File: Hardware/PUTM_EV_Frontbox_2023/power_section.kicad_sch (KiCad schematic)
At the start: 40 parts, among them U19 TLV743P, U4 TLV743P, U5 TLV743P, U7 LM62440-Q1

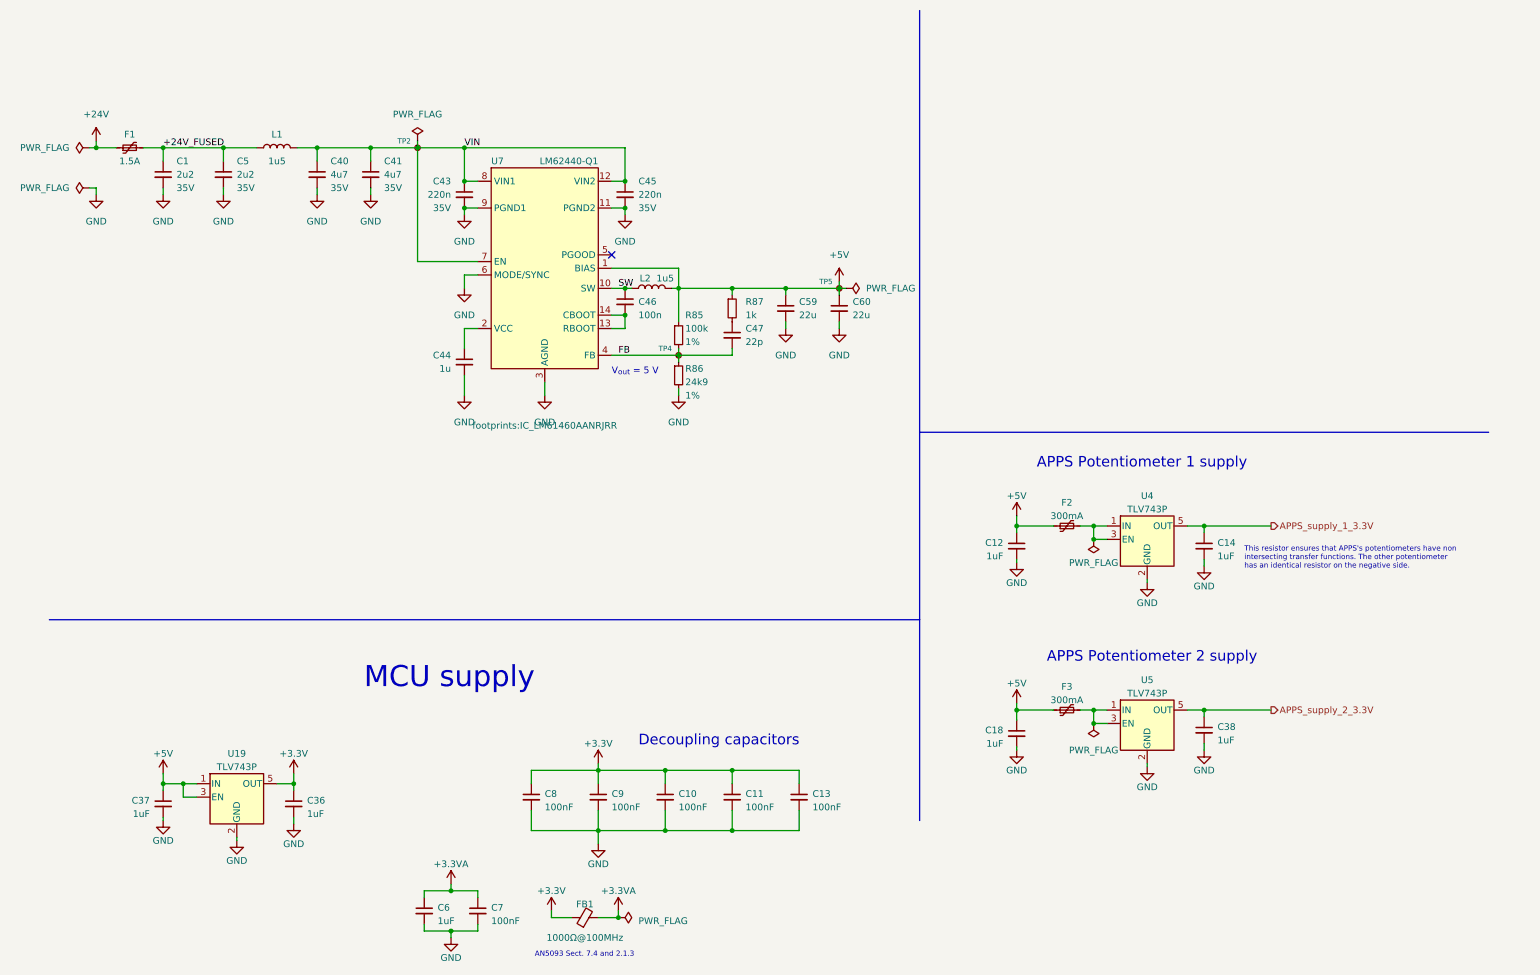
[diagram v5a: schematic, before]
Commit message: Added gearbox temperature sensors on schematic
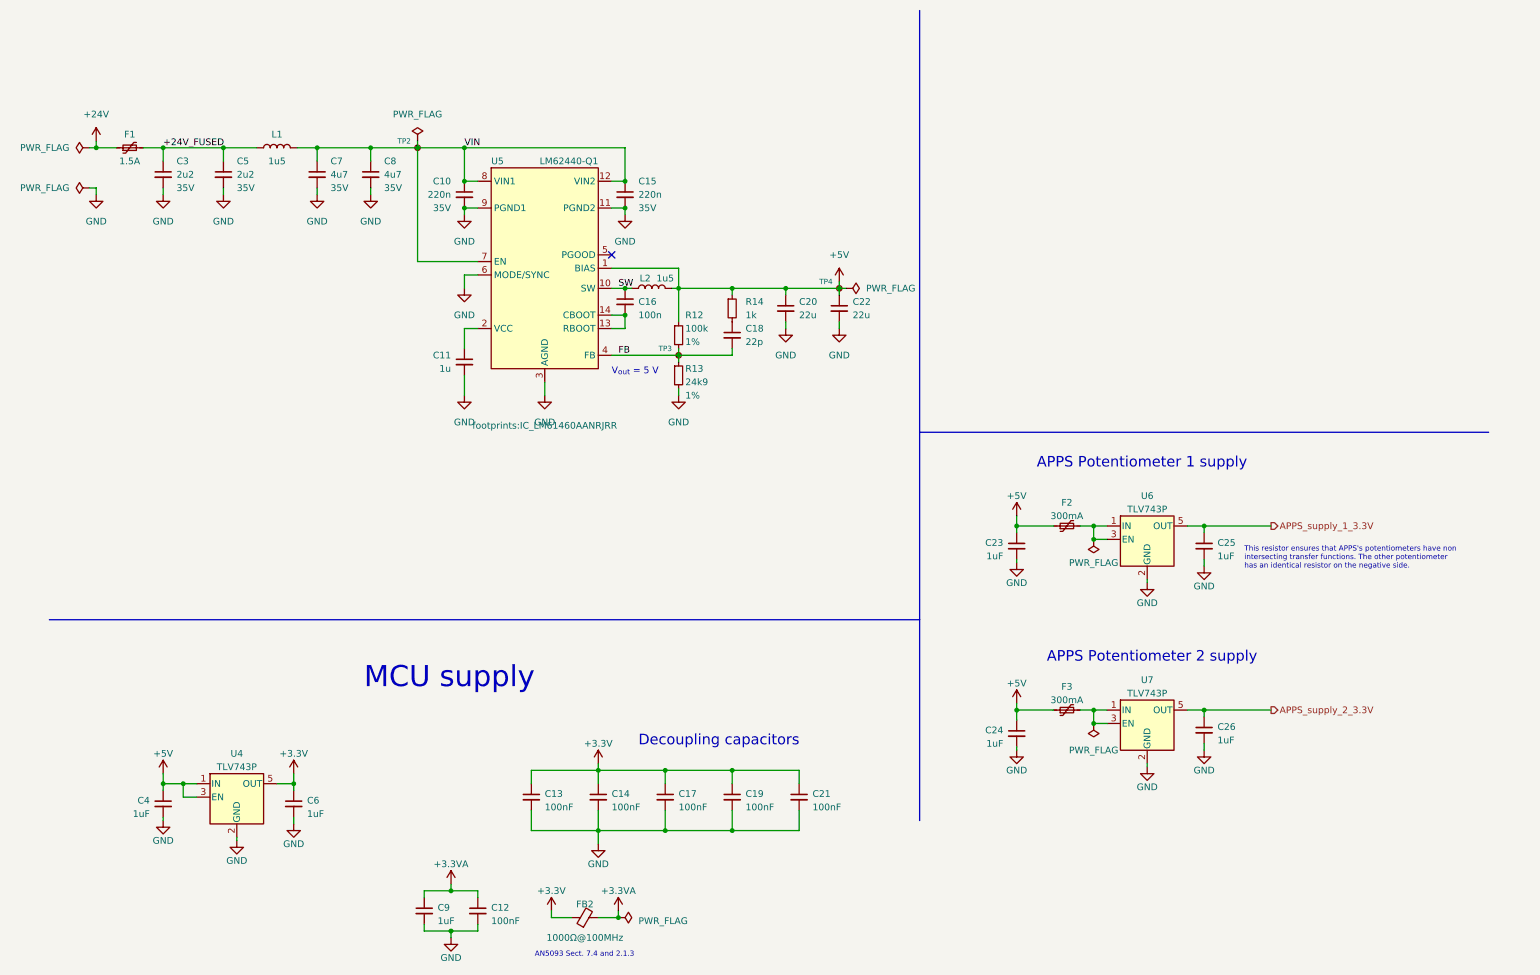
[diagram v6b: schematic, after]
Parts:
- renumbered C43 to C10, C44 to C11, C7 to C12, C8 to C13, C9 to C14, C45 to C15, C46 to C16, C10 to C17, C47 to C18, C11 to C19, C59 to C20, C13 to C21, C60 to C22, C12 to C23, C18 to C24, C14 to C25, C38 to C26, C1 to C3, C37 to C4, C36 to C6, C40 to C7, C41 to C8, C6 to C9, FB1 to FB2, R85 to R12, R86 to R13, R87 to R14, TP4 to TP3, TP5 to TP4, U19 to U4, U7 to U5, U4 to U6, U5 to U7
